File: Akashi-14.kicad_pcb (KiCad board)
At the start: 2 copper layers, 67.3 x 91.4 mm, 2 parts, among them J1 Conn_02x35_Odd_Even, J2 Conn_02x35_Odd_Even

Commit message: Layout done
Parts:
- added C1: 0.1u, Capacitor_THT:C_Disc_D3.0mm_W1.6mm_P2.50mm, F.Cu at (130.8, 123.2)
- added J3: CONN_N7E50-Q516RB-50_3MM, MyFootprint:N7E50-Q516RB-50, F.Cu at (131.4, 131.7)
- added R1: 1k, Resistor_THT:R_Axial_DIN0207_L6.3mm_D2.5mm_P10.16mm_Horizontal, F.Cu at (142.2, 106.7)
- added R2: 1k, Resistor_THT:R_Axial_DIN0207_L6.3mm_D2.5mm_P10.16mm_Horizontal, F.Cu at (138.4, 106.7)
- added R3: 1k, Resistor_THT:R_Axial_DIN0207_L6.3mm_D2.5mm_P10.16mm_Horizontal, F.Cu at (128.3, 106.7)
- added R4: 1k, Resistor_THT:R_Axial_DIN0207_L6.3mm_D2.5mm_P10.16mm_Horizontal, F.Cu at (123.2, 106.7)
- added TP1: Conn_01x09_Pin, Connector_PinHeader_2.54mm:PinHeader_1x09_P2.54mm_Vertical, F.Cu at (149.9, 95.2)
- added TP2: Conn_01x09_Pin, Connector_PinHeader_2.54mm:PinHeader_1x09_P2.54mm_Vertical, F.Cu at (113.0, 95.2)
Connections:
- J1 pad 28: /WAKEUP -> unconnected-(J1-Pin_28-Pad28)
- J1 pad 32: /IRQ -> unconnected-(J1-Pin_32-Pad32)
- J1 pad 39: /nOE -> /nIORD
- J1 pad 4: unconnected-(J1-Pin_4-Pad4) -> /IRQ
- J1 pad 41: /nWE -> /nIOWR
- J1 pad 43: unconnected-(J1-Pin_43-Pad43) -> /nWAIT
- J1 pad 53: unconnected-(J1-Pin_53-Pad53) -> /A0
- J1 pad 69: /D14 -> unconnected-(J1-Pin_69-Pad69)
- J2 pad 10: /D13 -> unconnected-(J2-Pin_10-Pad10)
- J2 pad 19: /nE1 -> unconnected-(J2-Pin_19-Pad19)
- J2 pad 2: unconnected-(J2-Pin_2-Pad2) -> /nCS0
- J2 pad 36: /A5 -> unconnected-(J2-Pin_36-Pad36)
- J2 pad 38: /A4 -> unconnected-(J2-Pin_38-Pad38)
- J2 pad 49: /D9 -> unconnected-(J2-Pin_49-Pad49)
- J2 pad 51: /D11 -> unconnected-(J2-Pin_51-Pad51)
- J2 pad 53: /D12 -> unconnected-(J2-Pin_53-Pad53)
- J2 pad 55: /D10 -> unconnected-(J2-Pin_55-Pad55)
- J2 pad 56: /D8 -> unconnected-(J2-Pin_56-Pad56)
- J2 pad 57: /A7 -> unconnected-(J2-Pin_57-Pad57)
- J2 pad 58: /A3 -> unconnected-(J2-Pin_58-Pad58)
- J2 pad 59: /A6 -> unconnected-(J2-Pin_59-Pad59)
- J2 pad 65: /D15 -> unconnected-(J2-Pin_65-Pad65)
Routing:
- net GND: track 0.00 -> 103.7 mm, vias 0 -> 22
- net /nCS0: track 0.00 -> 96.2 mm
- net /IRQ: track 0.00 -> 85.8 mm
- net /nWAIT: track 0.00 -> 84.4 mm
- net /D2: track 0.00 -> 79.1 mm
- net /D0: track 0.00 -> 68.4 mm
- net /D3: track 0.00 -> 66.4 mm, vias 0 -> 1
- net /D4: track 0.00 -> 66.3 mm, vias 0 -> 1
- net /A0: track 0.00 -> 66.3 mm
- net /nIORD: track 0.00 -> 65.3 mm
- net /D1: track 0.00 -> 65.2 mm
- net /nIOWR: track 0.00 -> 61.9 mm
- net /D6: track 0.00 -> 61.6 mm, vias 0 -> 1
- net /nRESET: track 0.00 -> 60.7 mm
- net /A1: track 0.00 -> 60.7 mm, vias 0 -> 1
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
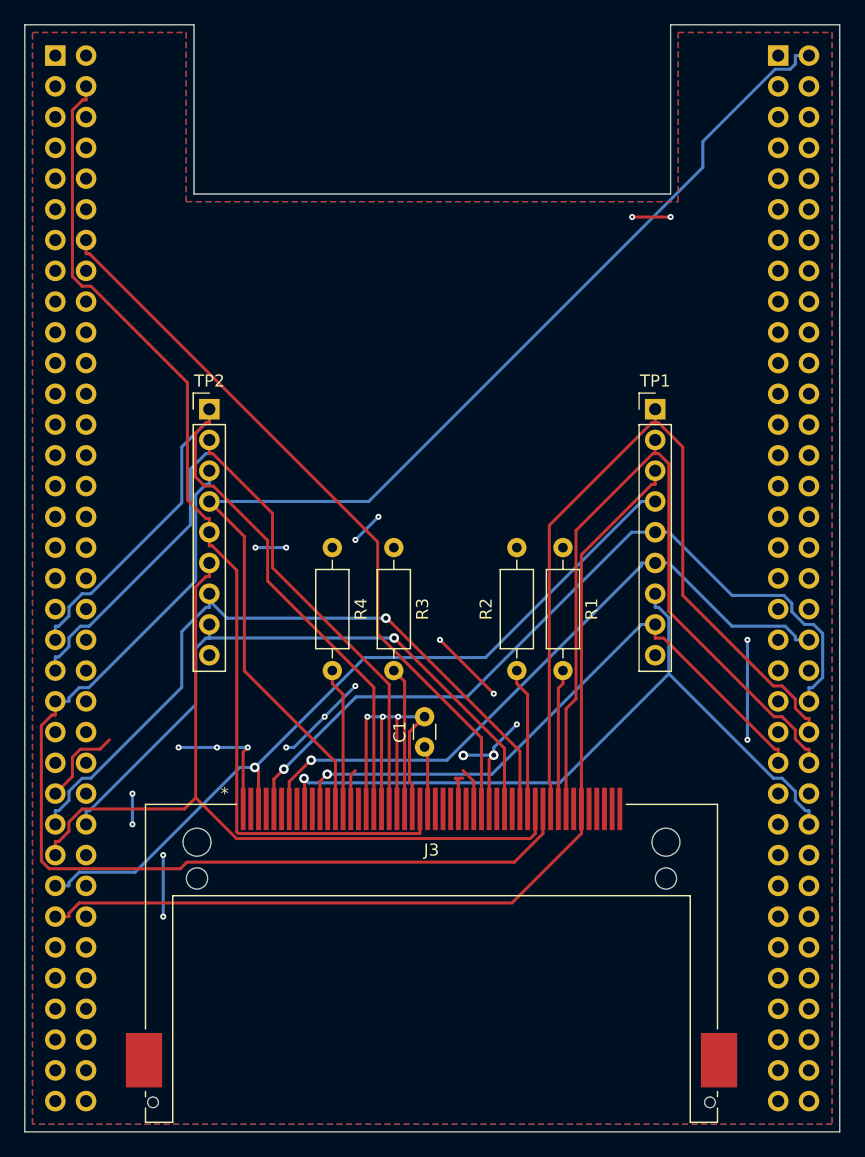
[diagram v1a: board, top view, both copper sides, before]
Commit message: Add text to the boad
Comment on the test point.
Name and compy right.
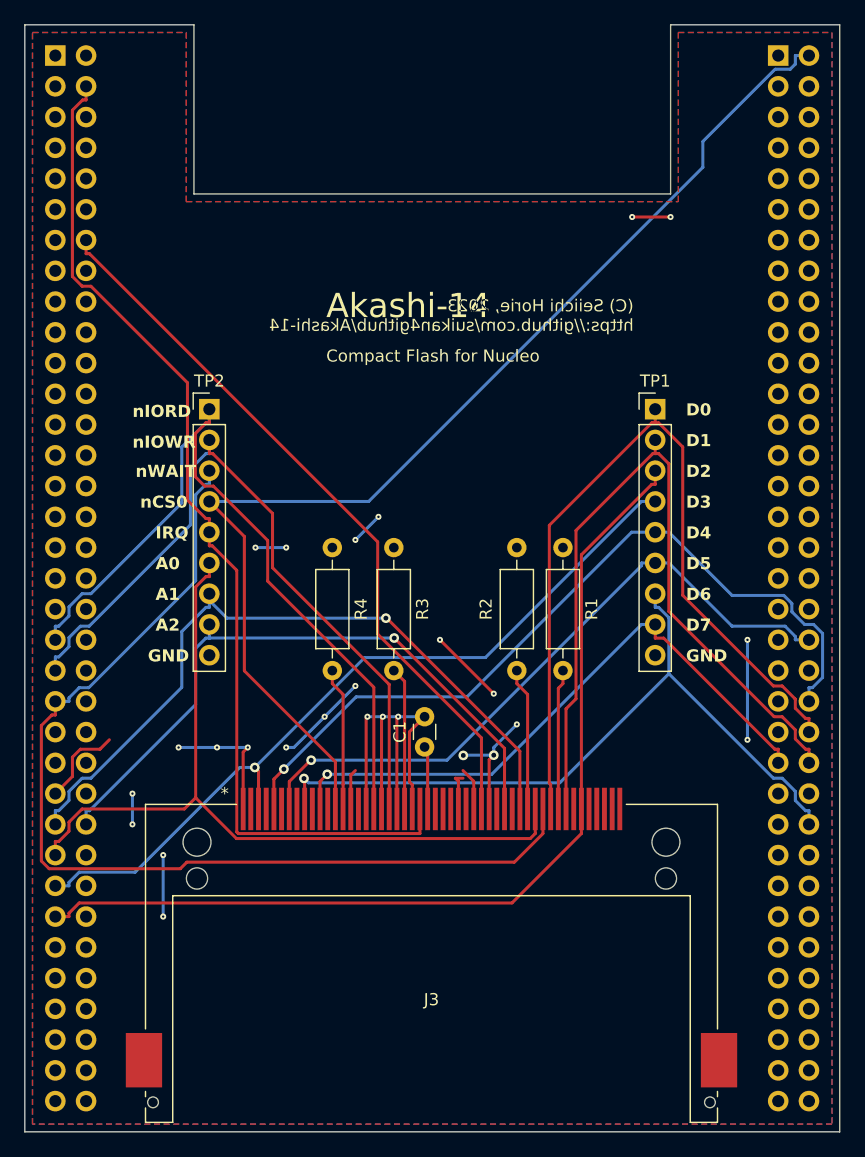
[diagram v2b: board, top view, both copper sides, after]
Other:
- board text added: "(C) Seiichi Horie, 2023 https://github.com/suikan4github/Akashi-14"
- board text added: "A0"
- board text added: "A1"
- board text added: "A2"
- board text added: "Akashi-14"
- board text added: "Compact Flash for Nucleo"
- board text added: "D0"
- board text added: "D1"
- board text added: "D2"
- board text added: "D3"
- board text added: "D4"
- board text added: "D5"
- board text added: "D6"
- board text added: "D7"
- board text added: "GND"
- board text added: "IRQ"
- board text added: "nCS0"
- board text added: "nIORD"
- board text added: "nIOWR"
- board text added: "nWAIT"
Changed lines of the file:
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@@
     (property "Sheetname" "")
     (attr through_hole)
-    (fp_text reference "J3" (at 0 0) (layer "F.SilkS")
+    (fp_text reference "J3" (at 0 12.357) (layer "F.SilkS")
         (effects (font (size 1 1) (thickness 0.15)))
     )
@@
   (gr_line (start 151.13 77.47) (end 111.76 77.47)
     (stroke (width 0.1) (type default)) (layer "Edge.Cuts"))
+  (gr_text "A1" (at 108.585 111.125) (layer "F.SilkS")
+    (effects (font (size 1 1) (thickness 0.2) bold) (justify left bottom))
+  )
+  (gr_text "D1" (at 152.4 98.425) (layer "F.SilkS")
+    (effects (font (size 1 1) (thickness 0.2) bold) (justify left bottom))
+  )
+  (gr_text "D5" (at 152.4 108.585) (layer "F.SilkS")
+    (effects (font (size 1 1) (thickness 0.2) bold) (justify left bottom))
+  )
+  (gr_text "D3" (at 152.4 103.505) (layer "F.SilkS")
+    (effects (font (size 1 1) (thickness 0.2) bold) (justify left bottom))
+  )
+  (gr_text "D4" (at 152.4 106.045) (layer "F.SilkS")
+    (effects (font (size 1 1) (thickness 0.2) bold) (justify left bottom))
+  )
+  (gr_text "nIORD" (at 106.68 96.012) (layer "F.SilkS")
+    (effects (font (size 1 1) (thickness 0.2) bold) (justify left bottom))
+  )
+  (gr_text "GND" (at 152.4 116.205) (layer "F.SilkS")
+    (effects (font (size 1 1) (thickness 0.2) bold) (justify left bottom))
+  )
+  (gr_text "A2" (at 108.585 113.665) (layer "F.SilkS")
+    (effects (font (size 1 1) (thickness 0.2) bold) (justify left bottom))
+  )
+  (gr_text "D6" (at 152.4 111.125) (layer "F.SilkS")
+    (effects (font (size 1 1) (thickness 0.2) bold) (justify left bottom))
+  )
+  (gr_text "D2" (at 152.4 100.965) (layer "F.SilkS")
+    (effects (font (size 1 1) (thickness 0.2) bold) (justify left bottom))
+  )
+  (gr_text "Compact Flash for Nucleo" (at 122.682 91.44) (layer "F.SilkS")
+    (effects (font (size 1 1) (thickness 0.15)) (justify left bottom))
+  )
+  (gr_text "A0" (at 108.585 108.585) (layer "F.SilkS")
+    (effects (font (size 1 1) (thickness 0.2) bold) (justify left bottom))
+  )
+  (gr_text "(C) Seiichi Horie, 2023\nhttps://github.com/suikan4github/Akashi-14" (at 148.082 88.9) (layer "F.SilkS")
+    (effects (font (size 1 1) (thickness 0.15)) (justify left bottom mirror))
+  )
+  (gr_text "D7" (at 152.4 113.665) (layer "F.SilkS")
+    (effects (font (size 1 1) (thickness 0.2) bold) (justify left bottom))
+  )
+  (gr_text "Akashi-14" (at 122.682 87.884) (layer "F.SilkS")
+    (effects (font (size 2 2) (thickness 0.25)) (justify left bottom))
+  )
+  (gr_text "D0" (at 152.4 95.885) (layer "F.SilkS")
+    (effects (font (size 1 1) (thickness 0.2) bold) (justify left bottom))
+  )
+  (gr_text "nWAIT" (at 106.934 100.965) (layer "F.SilkS")
+    (effects (font (size 1 1) (thickness 0.2) bold) (justify left bottom))
+  )
+  (gr_text "nIOWR" (at 106.68 98.552) (layer "F.SilkS")
+    (effects (font (size 1 1) (thickness 0.2) bold) (justify left bottom))
+  )
+  (gr_text "nCS0" (at 107.315 103.505) (layer "F.SilkS")
+    (effects (font (size 1 1) (thickness 0.2) bold) (justify left bottom))
+  )
+  (gr_text "GND" (at 107.95 116.205) (layer "F.SilkS")
+    (effects (font (size 1 1) (thickness 0.2) bold) (justify left bottom))
+  )
+  (gr_text "IRQ" (at 108.585 106.045) (layer "F.SilkS")
+    (effects (font (size 1 1) (thickness 0.2) bold) (justify left bottom))
+  )
   (dimension (type aligned) (layer "Cmts.User")
     (pts (xy 100.33 132.08) (xy 132.08 132.08))
     (height 35.56)
-    (gr_text "1250.0000 mils" (at 116.205 166.49) (layer "Cmts.User")
+    (gr_text "31.7500 mm" (at 116.205 166.49) (layer "Cmts.User")
       (effects (font (size 1 1) (thickness 0.15)))
     )
@@
     (pts (xy 100.33 151.13) (xy 163.83 151.13))
     (height 11.43)
-    (gr_text "2500.0000 mils" (at 132.08 160.76) (layer "Cmts.User")
+    (gr_text "63.5000 mm" (at 132.08 160.76) (layer "Cmts.User")
       (effects (font (size 1.5 1.5) (thickness 0.3)))
     )
@@
     (pts (xy 165.1 154.94) (xy 165.1 63.5))
     (height 4.15)
-    (gr_text "3600.0000 mils" (at 168.1 109.22 90) (layer "Cmts.User")
+    (gr_text "91.4400 mm" (at 168.1 109.22 90) (layer "Cmts.User")
       (effects (font (size 1 1) (thickness 0.15)))
     )
